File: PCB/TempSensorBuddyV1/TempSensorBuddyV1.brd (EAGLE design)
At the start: 11.9 x 15.7 mm, 8 parts, among them U1 MAX30205

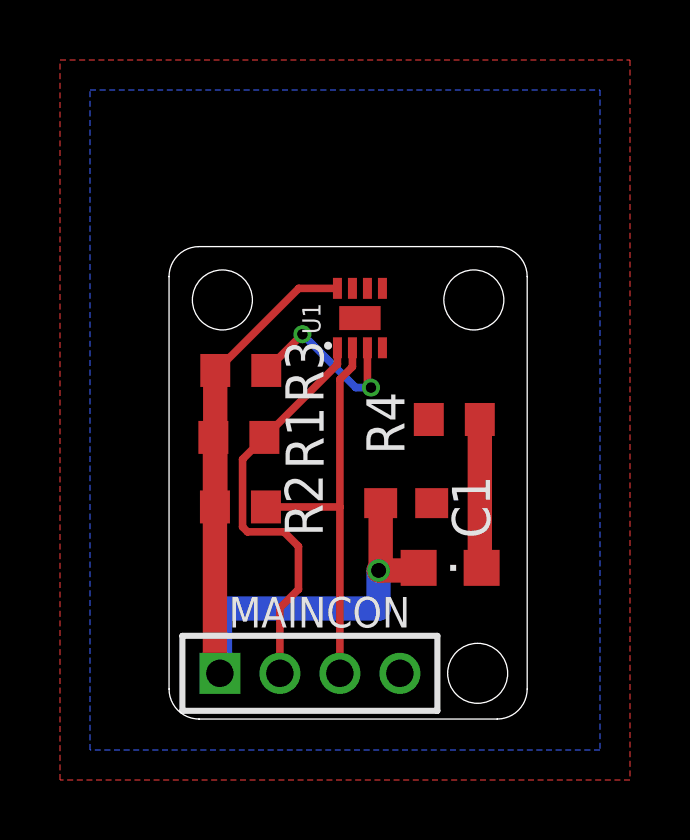
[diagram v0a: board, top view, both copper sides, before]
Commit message: Reviewed layout, added text, rounded corners. Design rule check passed. Ready for final review
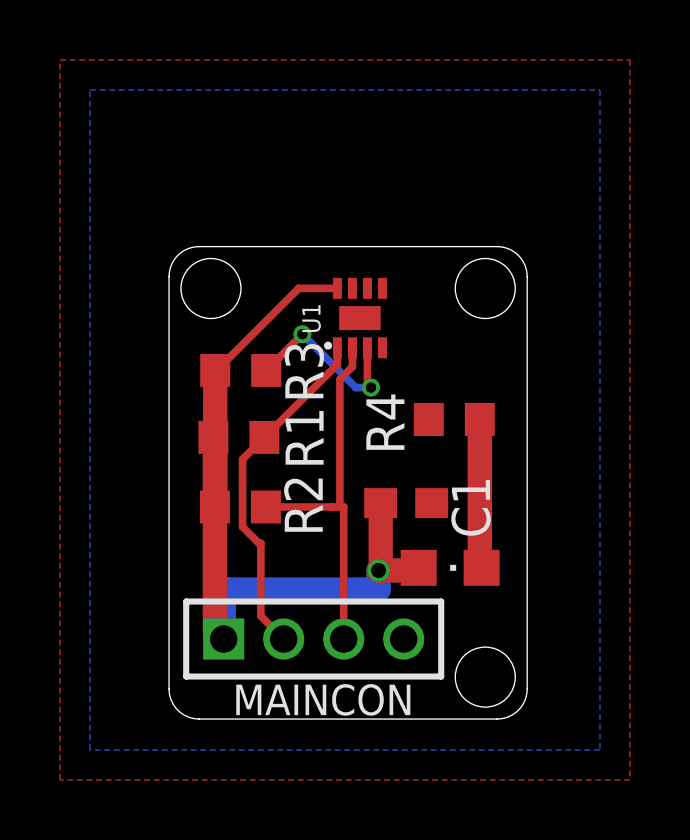
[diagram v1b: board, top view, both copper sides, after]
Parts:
- moved MAINCON 1.15 mm to (5.46, 4.70)
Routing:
- net +3V3: track 30.1 -> 27.7 mm
- net SDA: track 13.9 -> 11.6 mm
- net SCL: track 13.5 -> 12.5 mm
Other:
- board text added: "ES96"
- board text added: "Nicolas Weninger"
- board text added: "Temp Buddy"
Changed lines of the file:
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@@
 <drawing>
 <settings>
-<setting alwaysvectorfont="no"/>
+<setting alwaysvectorfont="yes"/>
 <setting verticaltext="up"/>
 </settings>
@@
 <layer number="27" name="tValues" color="7" fill="1" visible="yes" active="yes"/>
 <layer number="28" name="bValues" color="7" fill="1" visible="yes" active="yes"/>
-<layer number="29" name="tStop" color="7" fill="3" visible="no" active="yes"/>
+<layer number="29" name="tStop" color="7" fill="3" visible="yes" active="yes"/>
 <layer number="30" name="bStop" color="7" fill="6" visible="no" active="yes"/>
 <layer number="31" name="tCream" color="7" fill="4" visible="no" active="yes"/>
@@
 <wire x1="11.573" y1="17.78" x2="1.635" y2="17.78" width="0" layer="20"/>
 <wire x1="1.635" y1="17.78" x2="0.635" y2="16.78" width="0" layer="20" curve="90"/>
-<hole x="10.795" y="16.002" drill="2"/>
-<hole x="2.413" y="16.002" drill="2"/>
-<hole x="10.922" y="3.556" drill="2"/>
+<hole x="11.176" y="16.383" drill="2"/>
+<hole x="2.032" y="16.383" drill="2"/>
+<hole x="11.176" y="3.429" drill="2"/>
+<text x="9.652" y="15.367" size="1.778" layer="22" rot="MR0">ES96</text>
+<text x="6.731" y="12.065" size="1.27" layer="22" rot="MR0" align="center">Temp Buddy</text>
+<text x="6.35" y="9.271" size="1.27" layer="22" rot="MR0" align="center">Nicolas
+Weninger</text>
 </plain>
 <attributes>
@@
 <param name="mlMinCreamFrame" value="0mil"/>
 <param name="mlMaxCreamFrame" value="0mil"/>
-<param name="mlViaStopLimit" value="0mil"/>
+<param name="mlViaStopLimit" value="15mil"/>
 <param name="srRoundness" value="0"/>
 <param name="srMinRoundness" value="0mil"/>
@@
 <attribute name="SPICEPREFIX" value="C" x="31.4" y="-2.201" size="1.778" layer="27" display="off"/>
 </element>
-<element name="MAINCON" library="pinhead2" package="1X04M" value="" x="5.33" y="3.556" smashed="yes">
-<attribute name="NAME" x="8.674" y="6.1" size="1.016" layer="25" ratio="14" rot="R180"/>
-<attribute name="VALUE" x="11.33" y="2.556" size="0.8128" layer="27" ratio="10" rot="R90"/>
+<element name="MAINCON" library="pinhead2" package="1X04M" value="" x="5.457" y="4.699" smashed="yes">
+<attribute name="NAME" x="8.801" y="3.179" size="1.016" layer="25" ratio="14" rot="R180"/>
+<attribute name="VALUE" x="11.457" y="3.699" size="0.8128" layer="27" ratio="10" rot="R90"/>
 </element>
 <element name="PWR" library="led" library_urn="urn:adsk.eagle:library:259" package="CHIPLED_0805" package3d_urn="urn:adsk.eagle:package:15821/2" value="" x="10.005" y="7.071" smashed="yes" rot="R270">
@@
 <wire x1="7.69" y1="9.229" x2="7.69" y2="6.985" width="0.8128" layer="1"/>
 <wire x1="7.69" y1="6.985" x2="7.62" y2="6.985" width="0.8128" layer="1"/>
-<wire x1="7.62" y1="6.985" x2="7.62" y2="5.715" width="0.8128" layer="16"/>
-<wire x1="2.33" y1="5.715" x2="2.33" y2="3.556" width="0.8128" layer="16"/>
-<wire x1="7.62" y1="5.715" x2="2.33" y2="5.715" width="0.8128" layer="16"/>
+<wire x1="7.62" y1="6.985" x2="7.62" y2="6.35" width="0.8128" layer="16"/>
+<wire x1="2.457" y1="6.35" x2="2.457" y2="4.699" width="0.8128" layer="16"/>
+<wire x1="7.62" y1="6.35" x2="2.54" y2="6.35" width="0.8128" layer="16"/>
+<wire x1="2.54" y1="6.35" x2="2.457" y2="6.35" width="0.8128" layer="16"/>
 <wire x1="2.113" y1="11.419" x2="2.165" y2="11.419" width="0.8128" layer="1"/>
 <wire x1="2.165" y1="11.419" x2="2.165" y2="9.101" width="0.8128" layer="1"/>
@@
 <wire x1="2.221" y1="13.651" x2="2.175" y2="13.651" width="0.254" layer="1"/>
 <wire x1="4.958" y1="16.388" x2="2.221" y2="13.651" width="0.254" layer="1"/>
-<wire x1="2.165" y1="9.101" x2="2.165" y2="3.721" width="0.8128" layer="1"/>
-<wire x1="2.165" y1="3.721" x2="2.33" y2="3.556" width="0.8128" layer="1"/>
+<wire x1="2.165" y1="9.101" x2="2.165" y2="4.991" width="0.8128" layer="1"/>
+<wire x1="2.165" y1="4.991" x2="2.457" y2="4.699" width="0.8128" layer="1"/>
 <wire x1="8.955" y1="7.071" x2="8.869" y2="6.985" width="0.8128" layer="1"/>
 <wire x1="8.869" y1="6.985" x2="7.69" y2="6.985" width="0.8128" layer="1"/>
@@
 <contactref element="U1" pad="6"/>
 <contactref element="U1" pad="7"/>
-<polygon width="0.1524" layer="16">
+<polygon width="0.1524" layer="16" orphans="yes">
 <vertex x="-2" y="23"/>
 <vertex x="15" y="23"/>
@@
 <vertex x="-2" y="1"/>
 </polygon>
-<polygon width="0.1524" layer="1">
+<polygon width="0.1524" layer="1" orphans="yes">
 <vertex x="-3" y="24"/>
 <vertex x="16" y="24"/>
@@
 <wire x1="6.748" y1="13.773" x2="6.33" y2="13.355" width="0.254" layer="1"/>
 <wire x1="6.33" y1="13.355" x2="6.33" y2="9.101" width="0.254" layer="1"/>
-<wire x1="3.865" y1="9.101" x2="6.33" y2="9.101" width="0.254" layer="1"/>
-<wire x1="6.33" y1="9.101" x2="6.33" y2="3.556" width="0.254" layer="1"/>
+<wire x1="3.865" y1="9.101" x2="6.076" y2="9.101" width="0.254" layer="1"/>
+<wire x1="6.33" y1="9.101" x2="6.457" y2="9.101" width="0.254" layer="1"/>
+<wire x1="6.076" y1="9.101" x2="6.33" y2="9.101" width="0.254" layer="1"/>
+<wire x1="6.457" y1="9.101" x2="6.457" y2="4.699" width="0.254" layer="1"/>
 </signal>
 <signal name="SDA">
@@
 <contactref element="R1" pad="1"/>
 <contactref element="U1" pad="1"/>
-<wire x1="4.9494" y1="6.35526875" x2="4.9494" y2="7.78673125" width="0.254" layer="1"/>
-<wire x1="3.24926875" y1="8.2716" x2="3.0856" y2="8.43526875" width="0.254" layer="1"/>
-<wire x1="4.33" y1="3.556" x2="4.33" y2="5.73586875" width="0.254" layer="1"/>
-<wire x1="4.33" y1="5.73586875" x2="4.9494" y2="6.35526875" width="0.254" layer="1"/>
-<wire x1="4.9494" y1="7.78673125" x2="4.46453125" y2="8.2716" width="0.254" layer="1"/>
-<wire x1="4.46453125" y1="8.2716" x2="3.24926875" y2="8.2716" width="0.254" layer="1"/>
+<wire x1="3.695" y1="7.8906" x2="3.695" y2="5.461" width="0.254" layer="1"/>
+<wire x1="4.457" y1="4.699" x2="3.695" y2="5.461" width="0.254" layer="1"/>
+<wire x1="3.63026875" y1="7.8906" x2="3.0856" y2="8.43526875" width="0.254" layer="1"/>
+<wire x1="3.695" y1="7.8906" x2="3.63026875" y2="7.8906" width="0.254" layer="1"/>
 <wire x1="3.0856" y1="10.6916" x2="3.813" y2="11.419" width="0.254" layer="1"/>
 <wire x1="3.0856" y1="8.43526875" x2="3.0856" y2="10.6916" width="0.254" layer="1"/>
@@
 </drawing>
 <compatibility>
+<note version="6.3" minversion="6.2.2" severity="warning">
+Since Version 6.2.2 text objects can contain more than one line,
+which will not be processed correctly with this version.
+</note>
 <note version="8.2" severity="warning">
 Since Version 8.2, EAGLE supports online libraries. The ids

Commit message: Ordered. Added CAM files. Added 3D desgn files for Fusion 360.
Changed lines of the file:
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@@
 </layers>
 <board>
+<fusionsync huburn="a.cGVyc29uYWw6dWUyYTQwNWMw" projecturn="a.cGVyc29uYWw6dWUyYTQwNWMwIzIwMTgxMTIyMTYxNjk0NTgx" f3durn="urn:adsk.wipprod:dm.lineage:Pz8pRR99QVKkJXaCvIpEdQ" pcbguid="5437612e-7b6c-4196-a993-c848b8381be6" lastpulledtime="" lastsyncedchangeguid="0f07735d-ef75-6560-6ffd-43bc7f8613bd"/>
 <plain>
 <wire x1="0.635" y1="16.78" x2="0.635" y2="3.032" width="0" layer="20"/>
@@
 <text x="6.35" y="9.271" size="1.27" layer="22" rot="MR0" align="center">Nicolas
 Weninger</text>
+<dimension x1="12.573" y1="16.78" x2="0.635" y2="16.78" x3="6.604" y3="19.05" textsize="1.778" layer="51" width="0.1" precision="1"/>
+<dimension x1="1.635" y1="17.78" x2="1.635" y2="2.032" x3="-1.905" y3="9.906" textsize="1.778" layer="51" width="0.1" precision="1"/>
 </plain>
 <attributes>
@@
 <vertex x="-3" y="0"/>
 </polygon>
+<via x="9.779" y="14.478" extent="1-16" drill="0.35"/>
+<via x="5.334" y="10.668" extent="1-16" drill="0.35"/>
+<via x="5.334" y="7.493" extent="1-16" drill="0.35"/>
+<via x="2.159" y="3.048" extent="1-16" drill="0.35"/>
+<via x="9.144" y="17.018" extent="1-16" drill="0.35"/>
+<via x="11.049" y="5.588" extent="1-16" drill="0.35"/>
 </signal>
 <signal name="SCL">
@@
 </note>
 <note version="8.3" severity="warning">
+Since Version 8.3, EAGLE supports Fusion synchronisation.
+This feature will not be available in this version and saving
+the document will break the link to the Fusion PCB feature.
+</note>
+<note version="8.3" severity="warning">
